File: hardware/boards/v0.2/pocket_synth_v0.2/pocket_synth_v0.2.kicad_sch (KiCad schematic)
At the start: 54 parts, among them J1 Conn_ARM_JTAG_SWD_10, J2 DEVICE, J3 AudioJack3, J4 AudioJack3, J5 AudioJack3, J6 AudioJack3, J7 DISPLAY, J8 Micro_SD_Card_Det2, J9 HOST, SW1 SW_Push, SW2 SW_Push, SW3 SW_Push, SW4 SW_Push, U1 STM32H743XIHx, U3 SDRAM, U4 STM32H753VIHx, U5 W25Q128JVS, Y1 32.768kHz, Y2 HSE

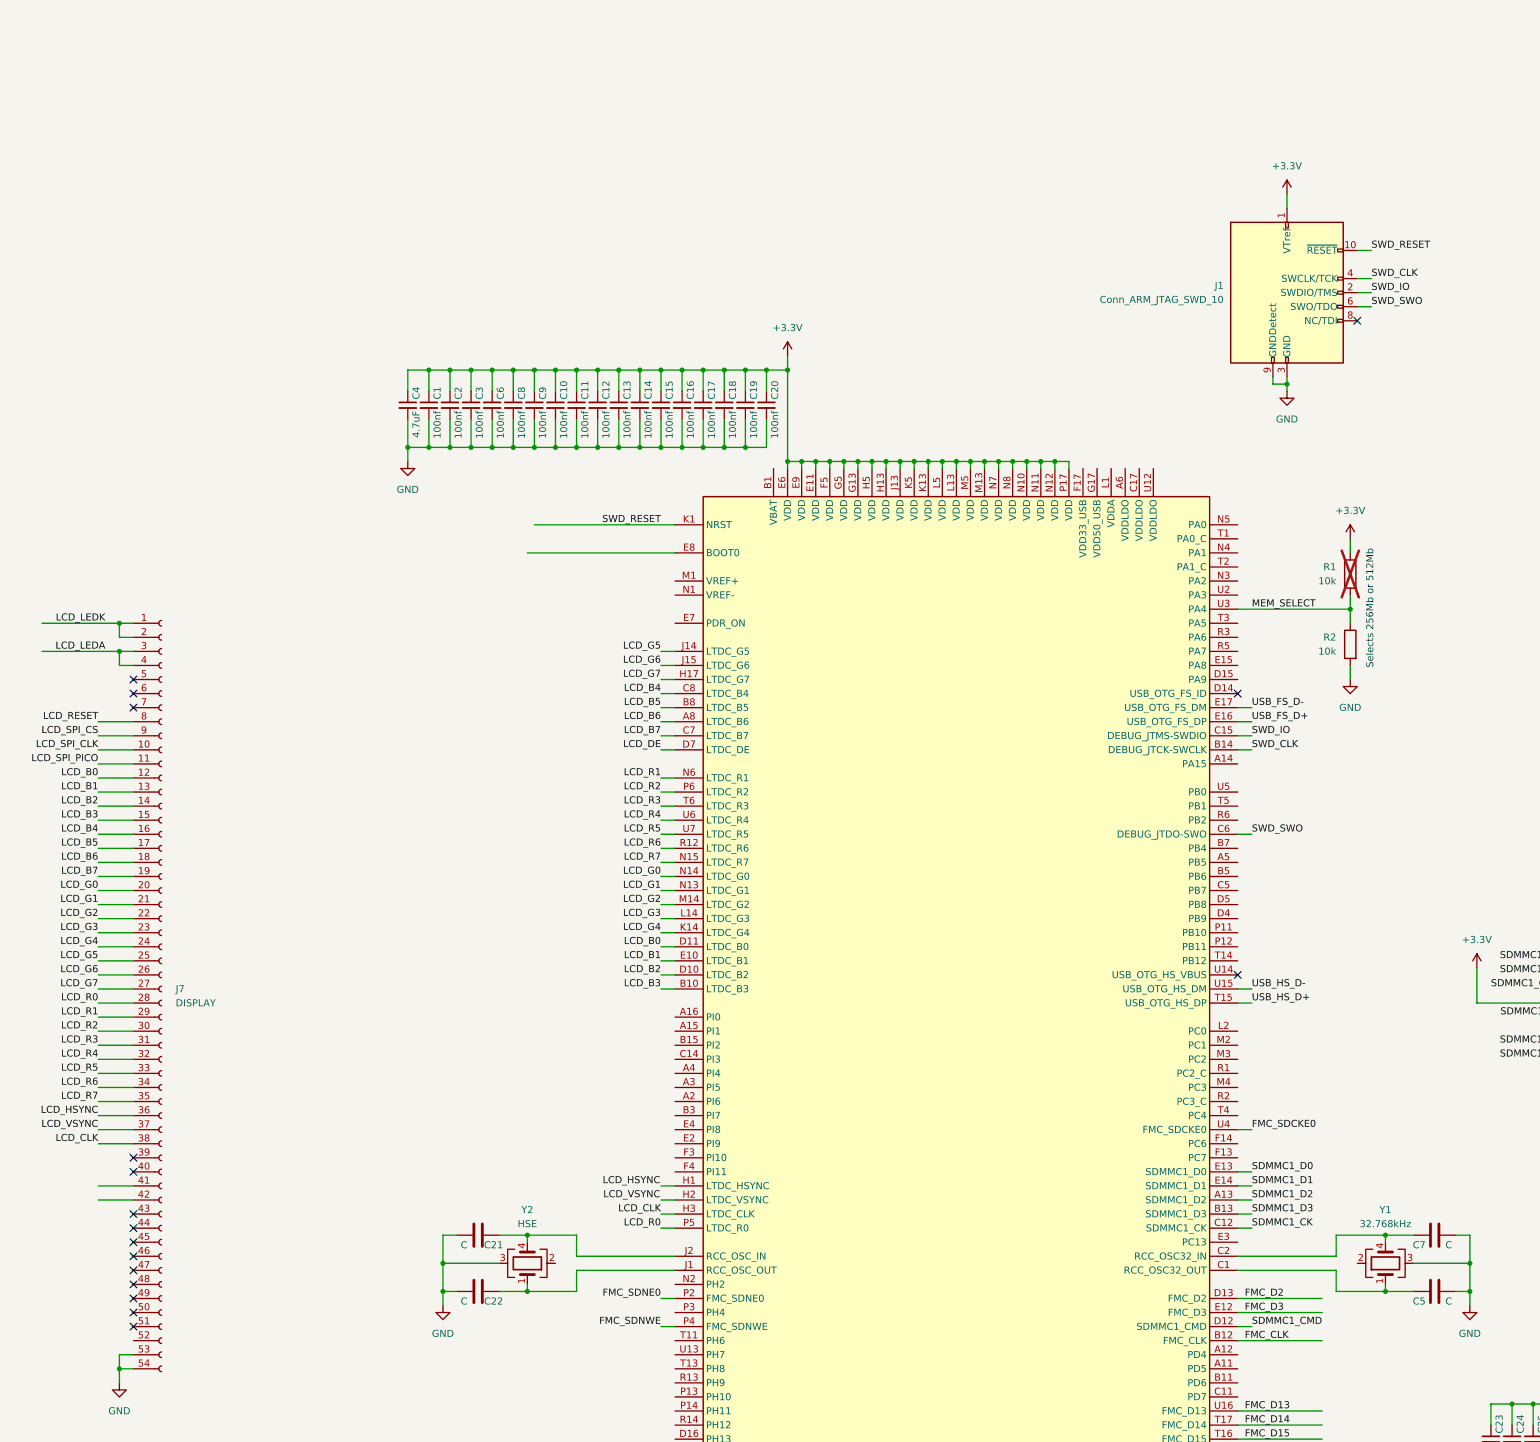
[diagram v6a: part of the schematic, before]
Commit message: more display connector routing
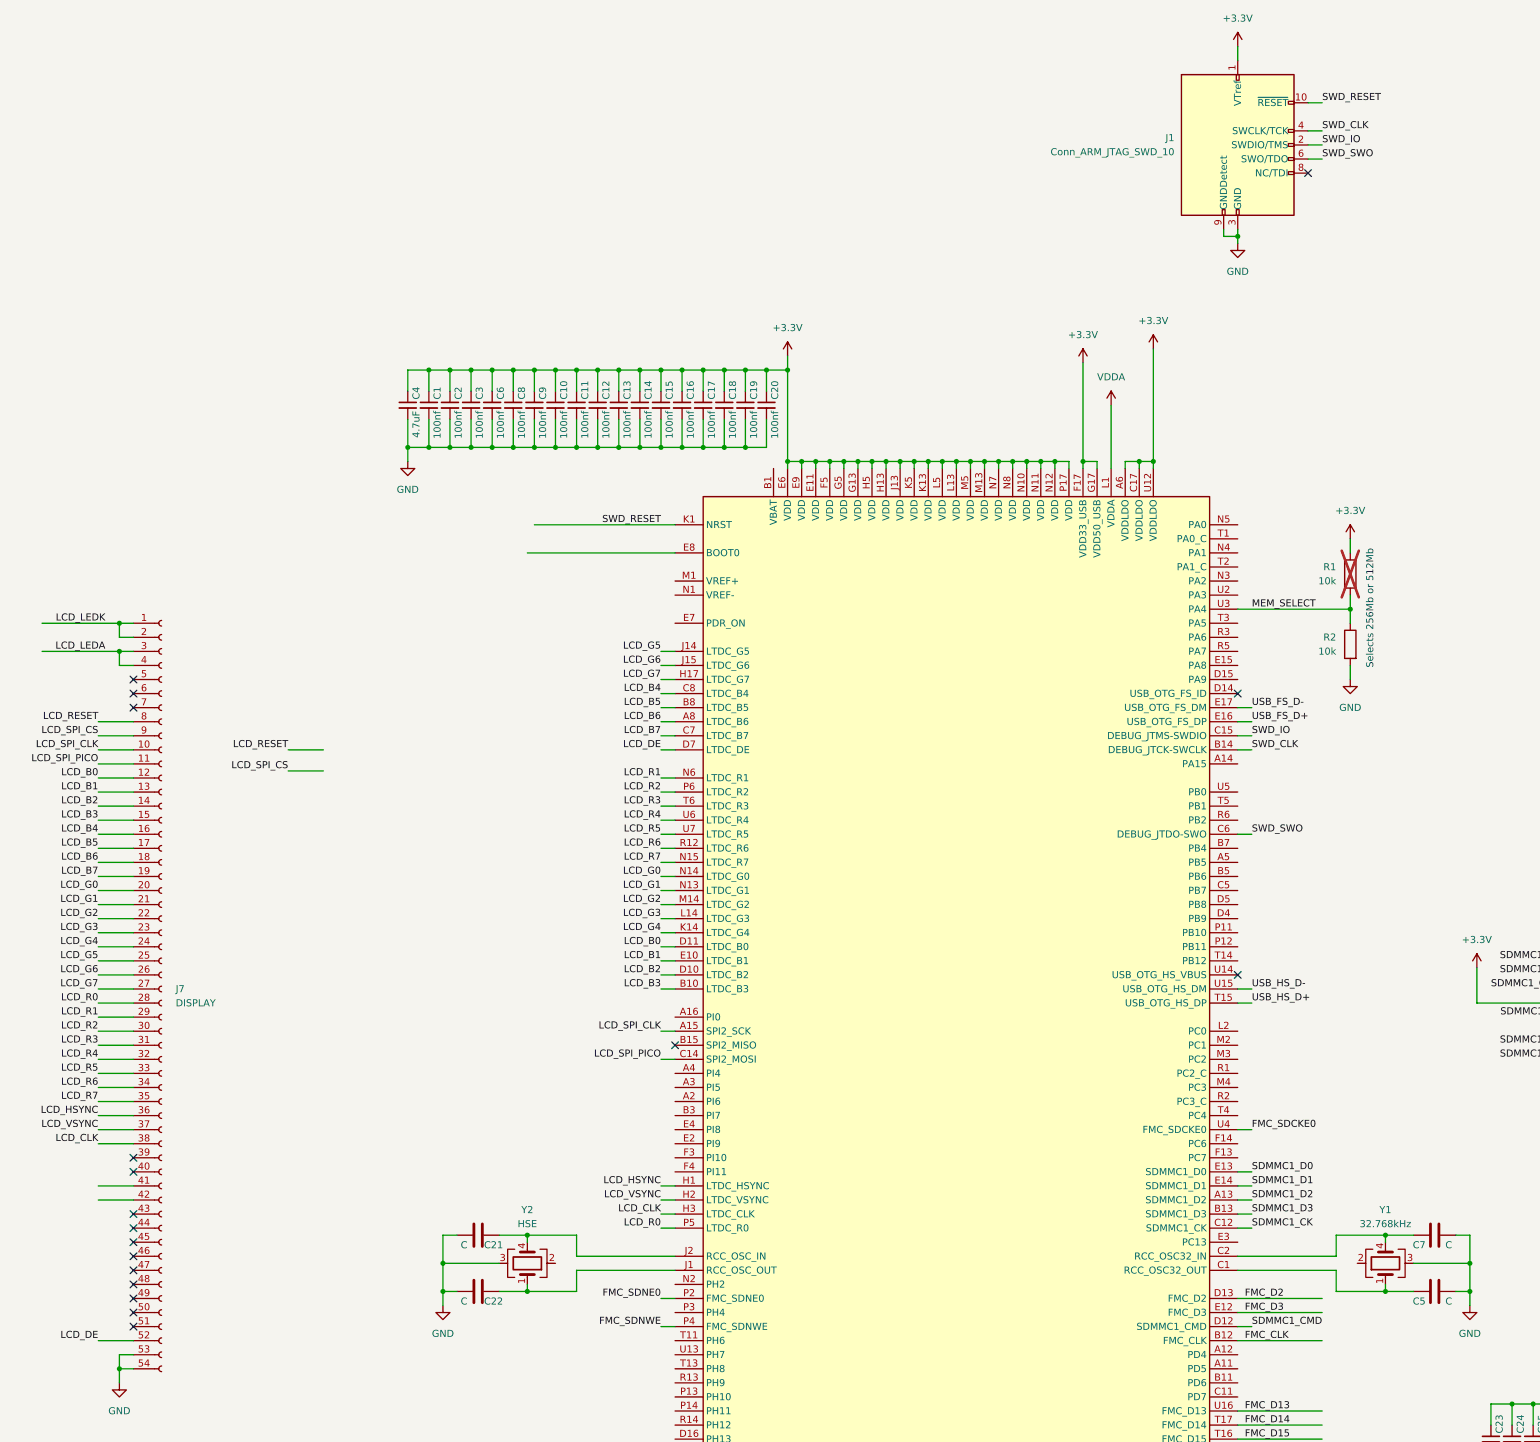
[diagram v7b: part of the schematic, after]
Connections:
- net +3.3V: now also U1.A6 (VDDLDO), U1.C17 (VDDLDO), U1.F17 (VDD33_USB), U1.G17 (VDD50_USB), U1.U12 (VDDLDO)
- net LCD_DE: now also J7.52 (Pin_52)
- net LCD_HSYNC: now also U1.H1 (PI12)
- net LCD_SPI_CLK: now also U1.A15 (PI1)
- net LCD_SPI_PICO: now also U1.C14 (PI3)
- net LCD_VSYNC: now also U1.H2 (PI13)
- net VDDA: now reaches U1.L1 (VDDA)
- no-connect marks 18 -> 19
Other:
- moved on the sheet: J1

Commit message: routing of various peripherals
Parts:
- removed J9: HOST, Connector_USB:USB_C_Receptacle_HCTL_HC-TYPE-C-16P-01A, symbol Connector:USB_C_Receptacle_USB2.0_16P
- added J10: Conn_01x05_Pin, Connector_PinHeader_1.00mm:PinHeader_1x05_P1.00mm_Vertical, symbol Connector:Conn_01x05_Pin
- added J11: Conn_01x02_Pin, Connector_PinHeader_1.00mm:PinHeader_1x02_P1.00mm_Vertical, symbol Connector:Conn_01x02_Pin
- added J12: Conn_01x03_Pin, Connector_PinHeader_1.00mm:PinHeader_1x03_P1.00mm_Vertical, symbol Connector:Conn_01x03_Pin
- added J13: INPUT, Connector_Hirose_DF40:Hirose_DF40C-20DS-0.4V_2x10_P0.4mm, symbol Connector_Generic:Conn_02x10_Odd_Even
- added J14: UART4, Connector_PinHeader_1.00mm:PinHeader_1x02_P1.00mm_Vertical, symbol Connector:Conn_01x02_Pin
- added J9: USART4, Connector_PinHeader_1.00mm:PinHeader_1x04_P1.00mm_Vertical, symbol Connector:Conn_01x04_Pin
- added R3: R, Resistor_SMD:R_0603_1608Metric, symbol Device:R
- J2: value DEVICE -> USB
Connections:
- net +3.3V: now also J7.41 (Pin_41), J7.42 (Pin_42)
- net GND: now also H1.1, H2.1, R3.2
- net LCD_RESET: now also U1.B16 (PH15), R3.1
- net LCD_SPI_CS: now also U1.A16 (PI0)
- net MEM_SELECT: no longer U1.U3 (PA4)
- net QSPI1_CS: now also U1.B5 (PB6); no longer U1.G15 (PG6)
- net at U1.B17 (PH14): now also J14.2 (Pin_2)
- net SAI1_MCLK_A: now reaches U1.C3 (PE2)
- net SAI1_MCLK_A: now also J10.1 (Pin_1)
- net SAI1_SCK_A: now reaches U1.D1 (PE5)
- net SAI1_SCK_A: now also J10.4 (Pin_4)
- net at U1.D14 (PA10): now also J9.2 (Pin_2)
- net at U1.D15 (PA9): now also J9.1 (Pin_1)
- net at U1.D16 (PH13): now also J14.1 (Pin_1)
- net SAI1_FS_A: now reaches U1.D2 (PE4)
- net SAI1_FS_A: now also J10.3 (Pin_3)
- net SAI1_SD_B: now reaches U1.D3 (PE3)
- net SAI1_SD_B: now also J10.2 (Pin_2)
- net SAI1_SD_A: now reaches U1.E5 (PE6)
- net SAI1_SD_A: now also J10.5 (Pin_5)
- net I2C4_SCL: now reaches U1.R16 (PD12)
- net I2C4_SCL: now also J11.1 (Pin_1)
- net I2C4_SDA: now reaches U1.R17 (PD13)
- net I2C4_SDA: now also J11.2 (Pin_2)
- net SPI1_MISO: now reaches U1.R3 (PA6)
- net SPI1_MISO: now also J12.2 (Pin_2)
- net SPI1_MOSI: now reaches U1.R5 (PA7)
- net SPI1_MOSI: now also J12.3 (Pin_3)
- net SPI1_SCK: now reaches U1.T3 (PA5)
- net SPI1_SCK: now also J12.1 (Pin_1)
- net USB_FS_D+: no longer names the net of U1.E16 (PA12)
- net USB_FS_D+: now also J9.4 (Pin_4)
- net USB_FS_D-: no longer names the net of U1.E17 (PA11)
- net USB_FS_D-: now also J9.3 (Pin_3)
- no-connect marks 19 -> 18
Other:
- note added: "Pull-down holds display in reset until the MCU is ready to initialize the display."
- moved on the sheet: C23, C24, C25, C26, C27, C28, C29, H2, R1, R2, U3
